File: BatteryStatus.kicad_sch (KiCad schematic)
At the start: 12 parts, among them J5 OLED DISPLAY, SW3 RotaryEncoder_Switch, U5 MAX17048G, U7 INA219BxD

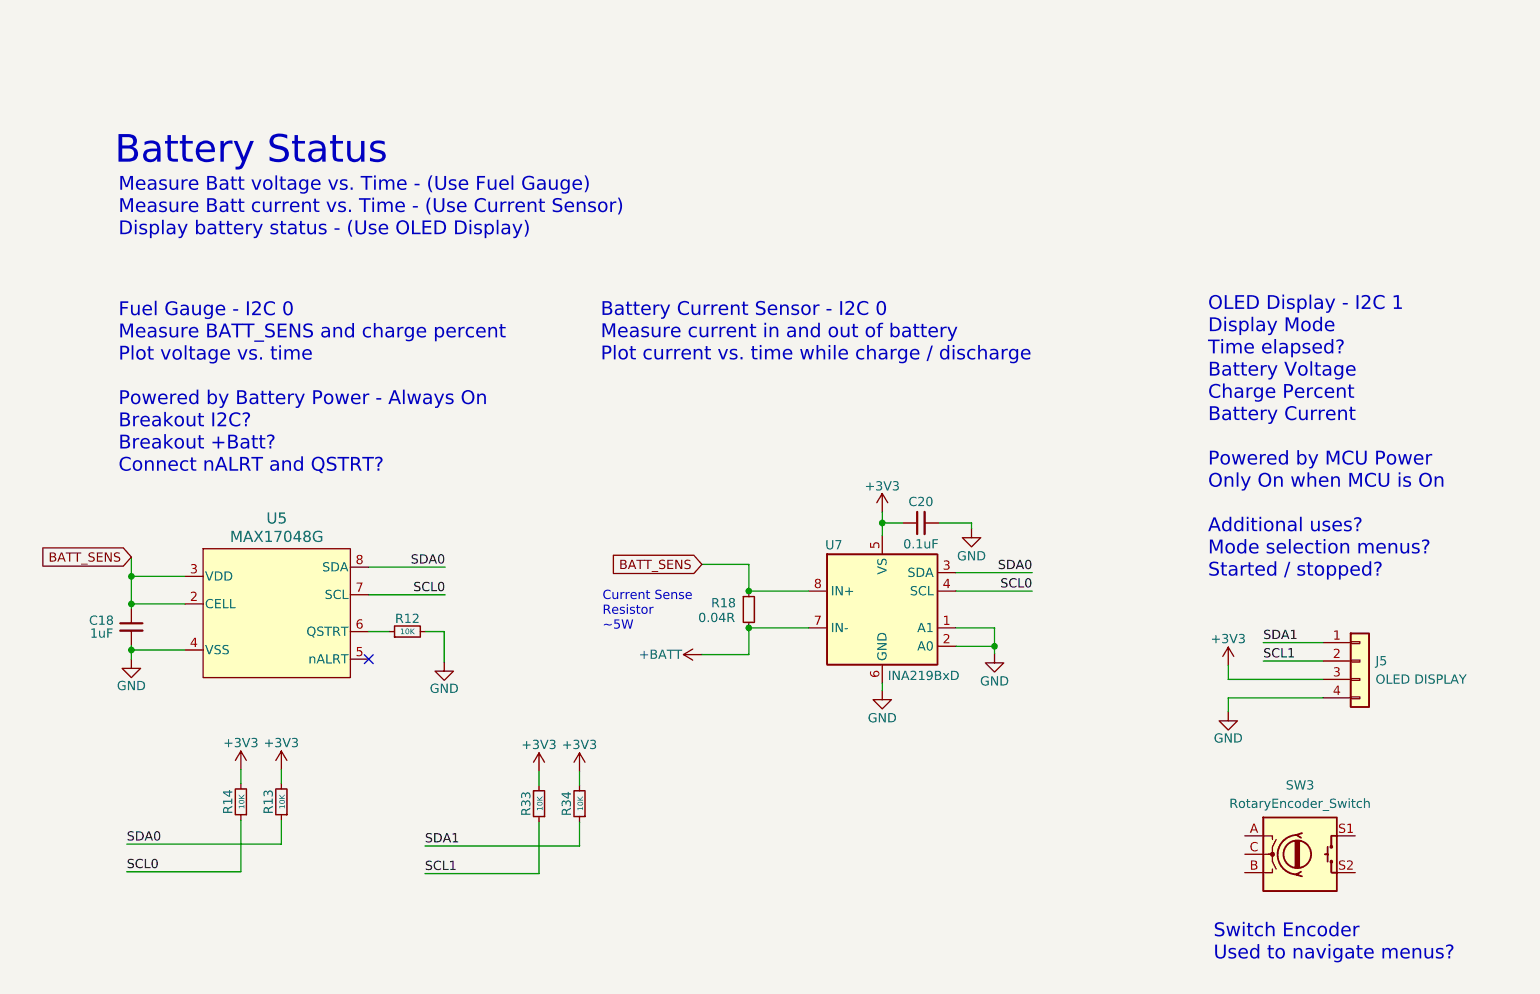
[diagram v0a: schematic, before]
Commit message: Finished Routing
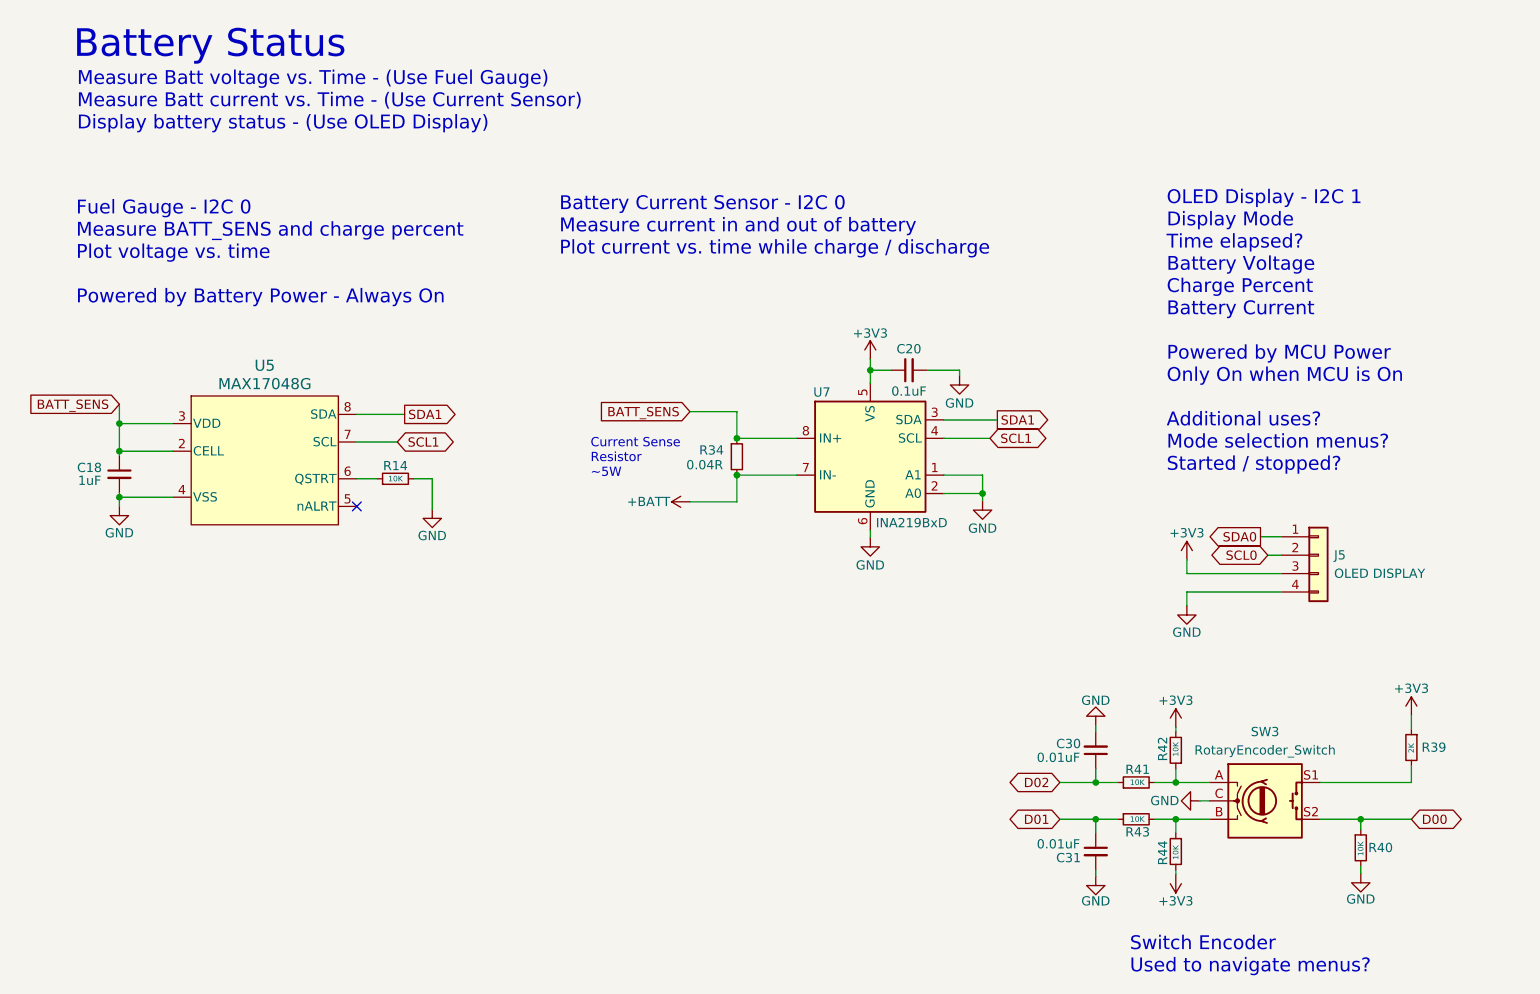
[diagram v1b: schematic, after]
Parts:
- removed R12, R13, R33: 10K, symbol Device:R_Small
- removed R18: 0.04R, Resistor_SMD:R_2512_6332Metric, symbol Device:R_Small
- added C30, C31: 0.01uF, Capacitor_SMD:C_0603_1608Metric, symbol Device:C_Small
- added R39: 2K, Resistor_SMD:R_0603_1608Metric, symbol Device:R_Small
- added R40, R41, R42, R43, R44: 10K, Resistor_SMD:R_0603_1608Metric, symbol Device:R_Small
- C18: footprint (none) -> Capacitor_SMD:C_0603_1608Metric
- J5: footprint (none) -> Connector_PinSocket_2.54mm:PinSocket_1x04_P2.54mm_Vertical
- R14: footprint (none) -> Resistor_SMD:R_0603_1608Metric
- R34: value 10K -> 0.04R; footprint (none) -> Resistor_SMD:R_2512_6332Metric
- SW3: footprint (none) -> Rotary_Encoder:RotaryEncoder_Alps_EC11E-Switch_Vertical_H20mm
- U5: footprint 21-0168E_T822-3_MXM -> BatteryTester:MAX17048G
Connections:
- net +3V3: now also R39.1, R42.2, R44.2; no longer R14.2, R34.2
- net +BATT: now also R34.2
- net BATT_SENS: now also R34.1
- net CTG: now also R14.2, SW3.C, C30.2, C31.2, R40.2
- net SCL0: now also J5.2 (Pin_2); no longer R14.1, U5.7 (SCL), U7.4 (SCL)
- net SCL1: now also U5.7 (SCL), U7.4 (SCL); no longer J5.2 (Pin_2)
- net SDA0: now also J5.1 (Pin_1); no longer U5.8 (SDA), U7.3 (SDA)
- net SDA1: now also U5.8 (SDA), U7.3 (SDA); no longer J5.1 (Pin_1), R34.1
- net at U5.6 (QSTRT): now also R14.1
- net at SW3.A: now also R41.2, R42.1
- net at SW3.B: now also R43.2, R44.1
- net at SW3.S1: now also R39.2
- net D00: now reaches SW3.S2
- net D00: now also R40.1
- new net D01: C31.1, R43.1
- new net D02: C30.1, R41.1
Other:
- note added: "Fuel Gauge - I2C 0 Measure BATT_SENS and charge percent Plot voltage vs. time Powered by Battery Power - Always On"
- note removed: "Fuel Gauge - I2C 0 Measure BATT_SENS and charge percent Plot voltage vs. time Powered by Battery Power - Always On Breakout I2C? Breakout +Batt? Connect nALRT and QSTRT?"
